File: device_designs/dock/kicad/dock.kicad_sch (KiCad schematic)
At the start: 16 parts, among them J1 USB_C_UPSTREAM, J2 USB_C_DS_x2, J3 USB_A_x2, J4 HDMI_or_DP, J5 RJ45, J6 RING_POGO, U1 JHL9040, U1A VL108, U2 TPS65994, U3 RTL8156, U4 VL817, U5 TPS55288RPMR, U6 TPS62864, U7 TLV75533PDRVR, U8 DWM3001C, U9 ALC4050

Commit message: fix(family): verify MPNs, freeze dock USB4/TB4, deepen mfg packages
Correct JHL9040R as TB4 retimer (not controller), freeze dock as USB4/TB4
40G with JHL8440, reject TB5, classify COM-HPC/NX5 pinout evidence, deepen
Gerber/STEP/PnP plans for all five, and document ring BOM↔FW parity.
KiCad brew needs Edmund admin — no COMPLETE claim.

Co-authored-by: Cursor <cursoragent@cursor.com>
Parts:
- added U1R: JHL9040R, symbol Device:R
- U1: value JHL9040 -> JHL8440; Role USB4_CONTROLLER -> USB4_TB4_DOCK_CONTROLLER
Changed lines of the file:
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@@
     (rev "0.2.0-dev")
     (company "gunnchOS3k / HARDWARE FAMILY DEPTH")
-    (comment 1 "ADR-FP-006 digital PCB package")
-    (comment 2 "USB4 + PD + hub + ring cradle")
+    (comment 1 "ADR-FP-006 + ADR-HW-002 USB4/TB4 40G NOT TB5")
+    (comment 2 "JHL8440 controller + JHL9040R retimer + PD + hub + cradle")
     (comment 3 "kicad-cli ABSENT → EDMUND_ACTION_REQUIRED")
     (comment 4 "PHYSICAL_EXECUTION_FREEZE ACTIVE — no fab, no purchase, draft digital only")
@@
     (in_bom yes) (on_board yes) (dnp no)
     (property "Reference" "U1" (at 40 33 0) (effects (font (size 1.27 1.27))))
-    (property "Value" "JHL9040" (at 40 47 0) (effects (font (size 1.27 1.27))))
+    (property "Value" "JHL8440" (at 40 47 0) (effects (font (size 1.27 1.27))))
     (property "Footprint" "" (at 40 40 0) (effects (font (size 1.27 1.27)) hide))
     (property "Datasheet" "" (at 40 40 0) (effects (font (size 1.27 1.27)) hide))
-    (property "Role" "USB4_CONTROLLER" (at 40 40 0) (effects (font (size 1.27 1.27)) hide))
+    (property "Role" "USB4_TB4_DOCK_CONTROLLER" (at 40 40 0) (effects (font (size 1.27 1.27)) hide))
+  )
+  (symbol (lib_id "Device:R") (at 65 40 0) (unit 1)
+    (in_bom yes) (on_board yes) (dnp no)
+    (property "Reference" "U1R" (at 65 33 0) (effects (font (size 1.27 1.27))))
+    (property "Value" "JHL9040R" (at 65 47 0) (effects (font (size 1.27 1.27))))
+    (property "Footprint" "" (at 65 40 0) (effects (font (size 1.27 1.27)) hide))
+    (property "Datasheet" "" (at 65 40 0) (effects (font (size 1.27 1.27)) hide))
+    (property "Role" "TB4_RETIMER" (at 65 40 0) (effects (font (size 1.27 1.27)) hide))
   )
   (symbol (lib_id "Device:R") (at 90 40 0) (unit 1)

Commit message: feat(eda): Cont VI KiCad 10.0.5 CLI validation + PCB load fixes
Install path resolved; run ERC/DRC/Gerber/drill/PnP/STEP for all five boards.
Fix KiCad 10 PCB load blockers (unknown setup key on Student/DS-XL; odd
5-layer copper on Dock → 4-layer). Record RING_KICAD_CLI_VALIDATION_PASS
and honest per-board violation counts; NDA release posture unchanged.

Co-authored-by: Cursor <cursoragent@cursor.com>
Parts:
- removed J2: USB_C_DS_x2, symbol Device:R
- removed J3: USB_A_x2, symbol Device:R
- added FORBID1: JHL9480, symbol Device:R
- added FORBID2: JHL9580, symbol Device:R
- added J2A, J2B: USB4085, symbol Device:R
- added J3A, J3B: USB3_A, symbol Device:R
- J1: value USB_C_UPSTREAM -> USB4085
- J4: value HDMI_or_DP -> HDMI_TypeA
- J5: value RJ45 -> JK0-0136NL
- J6: value RING_POGO -> Mill-Max_pogo
- U2: value TPS65994 -> TPS65994ADFBRQ1
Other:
- company: gunnchOS3k / HARDWARE FAMILY DEPTH -> gunnchOS3k / CONTINUATION VI
- title: Dock Main PCB — beyond skeleton -> Dock Main PCB — USB4/TB4 40G topology

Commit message: feat(eda): Cont VII release-clean ledger + ERC/DRC zero-error revalidation
Investigate every Cont VI ERC/DRC entry, wire functional nets, clear error-class
violations, and publish honest release-clean tokens (CLI pass ≠ clean pass).

Co-authored-by: Cursor <cursoragent@cursor.com>
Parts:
- removed FORBID1: JHL9480, symbol Device:R
- removed FORBID2: JHL9580, symbol Device:R
- removed J1, J2A, J2B: USB4085, symbol Device:R
- removed J3A, J3B: USB3_A, symbol Device:R
- removed J4: HDMI_TypeA, symbol Device:R
- removed J5: JK0-0136NL, symbol Device:R
- removed J6: Mill-Max_pogo, symbol Device:R
- removed U1: JHL8440, symbol Device:R
- removed U1A: VL108, symbol Device:R
- removed U1R: JHL9040R, symbol Device:R
- removed U2: TPS65994ADFBRQ1, symbol Device:R
- removed U3: RTL8156, symbol Device:R
- removed U4: VL817, symbol Device:R
- removed U5: TPS55288RPMR, symbol Device:R
- removed U6: TPS62864, symbol Device:R
- removed U7: TLV75533PDRVR, symbol Device:R
- removed U8: DWM3001C, symbol Device:R
- removed U9: ALC4050, symbol Device:R
- added FORBID1: JHL9480, gunnchos_structural:Block_SMD_10x10, symbol FuncBlock
- added FORBID2: JHL9580, gunnchos_structural:Block_SMD_10x10, symbol FuncBlock
- added J1, J2A, J2B: USB4085, gunnchos_structural:Block_SMD_10x10, symbol FuncBlock
- added J3A, J3B: USB3_A, gunnchos_structural:Block_SMD_10x10, symbol FuncBlock
- added J4: HDMI_TypeA, gunnchos_structural:Block_SMD_10x10, symbol FuncBlock
- added J5: JK0-0136NL, gunnchos_structural:Block_SMD_10x10, symbol FuncBlock
- added J6: Mill-Max_pogo, gunnchos_structural:Block_SMD_10x10, symbol FuncBlock
- added U1: JHL8440, gunnchos_structural:Block_SMD_10x10, symbol FuncBlock
- added U1A: VL108, gunnchos_structural:Block_SMD_10x10, symbol FuncBlock
- added U1R: JHL9040R, gunnchos_structural:Block_SMD_10x10, symbol FuncBlock
- added U2: TPS65994ADFBRQ1, gunnchos_structural:Block_SMD_10x10, symbol FuncBlock
- added U3: RTL8156, gunnchos_structural:Block_SMD_10x10, symbol FuncBlock
- added U4: VL817, gunnchos_structural:Block_SMD_10x10, symbol FuncBlock
- added U5: TPS55288RPMR, gunnchos_structural:Block_SMD_10x10, symbol FuncBlock
- added U6: TPS62864, gunnchos_structural:Block_SMD_10x10, symbol FuncBlock
- added U7: TLV75533PDRVR, gunnchos_structural:Block_SMD_10x10, symbol FuncBlock
- added U8: DWM3001C, gunnchos_structural:Block_SMD_10x10, symbol FuncBlock
- added U9: ALC4050, gunnchos_structural:Block_SMD_10x10, symbol FuncBlock
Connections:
- net CC1: now also J3A.2
- net CC2: now also J3B.2
- net HDMI_TX: now also U1.1
- net I2C_PD: now also J4.2
- net I2C_RETIMER: now also J5.2
- net MDI: now also FORBID2.2
- net RING_CHARGE_5V: now also U1R.1
- net SPI_UWB: now also U1A.1
- net SS_RX_DS1: now also J1.2
- net SS_RX_DS2: now also J2B.2
- net SS_RX_HOST: now also U6.2
- net SS_RX_UP: now also U8.2
- net SS_TX_DS1: now also U9.2
- net SS_TX_DS2: now also J2A.2
- net SS_TX_HOST: now also U5.2
- net SS_TX_UP: now also U7.2
- net USB_A1: now also J6.2
- net USB_A2: now also FORBID1.2
- net VBUS_DS1: now also U1R.2
- net VBUS_DS2: now also U1A.2
- net VBUS_UPSTREAM: now also U1.2
- net VDD_1V8: now also U4.2
- net VDD_3V3: now also U3.2
- net VSYS_5V: now also U2.2
- no-connect marks 0 -> 18
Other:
- company: gunnchOS3k / CONTINUATION VI -> gunnchOS3k / CONTINUATION VII
- title: Dock Main PCB — USB4/TB4 40G topology -> Dock Main PCB — USB4/TB4 Cont VII

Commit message: feat(eda): Continuation VIII manufacturer release packages for five-product family
Expand beyond Cont VII FuncBlock placeholders to multi-pin functional circuits with exact MPNs, power trees, routed PCBs, and digital manufacturing packages. Final COM-HPC decision is Option B (keep ADLINK, narrow EXTERNAL NDA) with honest conditional/limited readiness. ERC/DRC errors are zero on all five boards under KiCad 10.0.5; PHYSICAL_EXECUTION_FREEZE remains active.

Co-authored-by: Cursor <cursoragent@cursor.com>
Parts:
- removed FORBID1: JHL9480, gunnchos_structural:Block_SMD_10x10, symbol FuncBlock
- removed FORBID2: JHL9580, gunnchos_structural:Block_SMD_10x10, symbol FuncBlock
- removed J1, J2A, J2B: USB4085, gunnchos_structural:Block_SMD_10x10, symbol FuncBlock
- removed J3A, J3B: USB3_A, gunnchos_structural:Block_SMD_10x10, symbol FuncBlock
- removed J4: HDMI_TypeA, gunnchos_structural:Block_SMD_10x10, symbol FuncBlock
- removed J5: JK0-0136NL, gunnchos_structural:Block_SMD_10x10, symbol FuncBlock
- removed J6: Mill-Max_pogo, gunnchos_structural:Block_SMD_10x10, symbol FuncBlock
- removed U1: JHL8440, gunnchos_structural:Block_SMD_10x10, symbol FuncBlock
- removed U1A: VL108, gunnchos_structural:Block_SMD_10x10, symbol FuncBlock
- removed U1R: JHL9040R, gunnchos_structural:Block_SMD_10x10, symbol FuncBlock
- removed U2: TPS65994ADFBRQ1, gunnchos_structural:Block_SMD_10x10, symbol FuncBlock
- removed U3: RTL8156, gunnchos_structural:Block_SMD_10x10, symbol FuncBlock
- removed U4: VL817, gunnchos_structural:Block_SMD_10x10, symbol FuncBlock
- removed U5: TPS55288RPMR, gunnchos_structural:Block_SMD_10x10, symbol FuncBlock
- removed U6: TPS62864, gunnchos_structural:Block_SMD_10x10, symbol FuncBlock
- removed U7: TLV75533PDRVR, gunnchos_structural:Block_SMD_10x10, symbol FuncBlock
- removed U8: DWM3001C, gunnchos_structural:Block_SMD_10x10, symbol FuncBlock
- removed U9: ALC4050, gunnchos_structural:Block_SMD_10x10, symbol FuncBlock
- added C1: CL05A104KA5NNNC, gunnchos_functional:C_0402, symbol C
- added C2: GRM188R60J106ME47D, gunnchos_functional:C_0402, symbol C
- added D1: APTD1608LCGCK, gunnchos_functional:LED_0603, symbol LED
- added DESD1: PESD5V0S1UL, gunnchos_functional:R_0402, symbol C
- added JUSB1, JUSB2: TYPE-C-31-M-12, gunnchos_functional:Block_SMD_safe, symbol USB_C
- added R1: RC0402FR-0710KL, gunnchos_functional:R_0402, symbol R
- added R2: RC0402FR-071K0L, gunnchos_functional:R_0402, symbol R
- added U3V3: TPS62864, gunnchos_functional:Block_SMD_safe, symbol BUCK
- added UCHG1: BQ25792RQMR, gunnchos_functional:Block_SMD_safe, symbol CHARGER
- added UETH1: RTL8156, gunnchos_functional:Block_SMD_safe, symbol RTL8156
- added UHUB1: VL817, gunnchos_functional:Block_SMD_safe, symbol VL817
- added UPD1: TPS65994ADFBRQ1, gunnchos_functional:Block_SMD_safe, symbol PD_CTRL
- added UUSB4: JHL8440, gunnchos_functional:Block_SMD_safe, symbol JHL8440_ROLE
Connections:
- net CC1: now also DESD1.1, JUSB1.A5 (CC1), UPD1.8 (3V3)
- net VDD_3V3: now also C1.1, R1.1, R2.1, U3V3.2 (EN), U3V3.4 (VOUT), UETH1.7 (RD+), UHUB1.5 (DN1_DP), UPD1.2 (CC1), UUSB4.9 (NOTE_NDA)
- new net ETH_TD_N: UETH1.4 (USB_D-)
- new net ETH_TD_P: UETH1.3 (USB_D+)
- new net GND: C1.2, C2.2, D1.1 (K), DESD1.2, JUSB1.A7 (DM), JUSB2.A7 (DM), U3V3.1 (VIN), UCHG1.4 (GND), UETH1.8 (RD-), UHUB1.6 (DN1_DM), UPD1.6 (SDA), UUSB4.8 (I2C_SDA)
- new net HUB_DN1_DM: JUSB2.A1 (GND), UHUB1.2 (GND)
- new net HUB_DN1_DP: JUSB2.A6 (DP), UHUB1.1 (VDD)
- new net I2C_SCL: R1.2, UCHG1.1 (VBUS), UPD1.3 (CC2), UUSB4.3 (USB4_UP_RX)
- new net I2C_SDA: UCHG1.2 (SYS), UPD1.4 (GND), UUSB4.2 (GND)
- new net LED_A: D1.2 (A), R2.2
- new net USB4_UP: UUSB4.6 (PCIE_DN), UUSB4.7 (I2C_SCL)
- new net USB_DM: UETH1.6 (TD-), UHUB1.4 (UP_DM)
- new net USB_DP: UETH1.5 (TD+), UHUB1.3 (UP_DP)
- new net VBAT: UCHG1.3 (BAT)
- new net VBUS: JUSB1.B5 (CC2), JUSB2.B5 (CC2), UCHG1.5 (SCL), UPD1.7 (VSYS)
- new net VSYS: C2.1, U3V3.3 (GND), UCHG1.6 (SDA), UPD1.1 (VBUS)
- no-connect marks 18 -> 11
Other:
- note added: "Cont VIII functional schematic — multi-pin symbols + exact MPNs (not FuncBlock placeholders)."
- note added: "EXTERNAL_NDA_BLOCKED: Intel JHL8440 / JHL9040R package ball maps"
- note added: "Revision 0.5.0-cont-viii."
- note added: "SI notes encoded on PCB stackup/Dwgs — no SI simulation claimed."
- company: gunnchOS3k / CONTINUATION VII -> gunnchOS3k / CONTINUATION VIII
- title: Dock Main PCB — USB4/TB4 Cont VII -> Dock Main PCB — USB4/TB4 Cont VIII

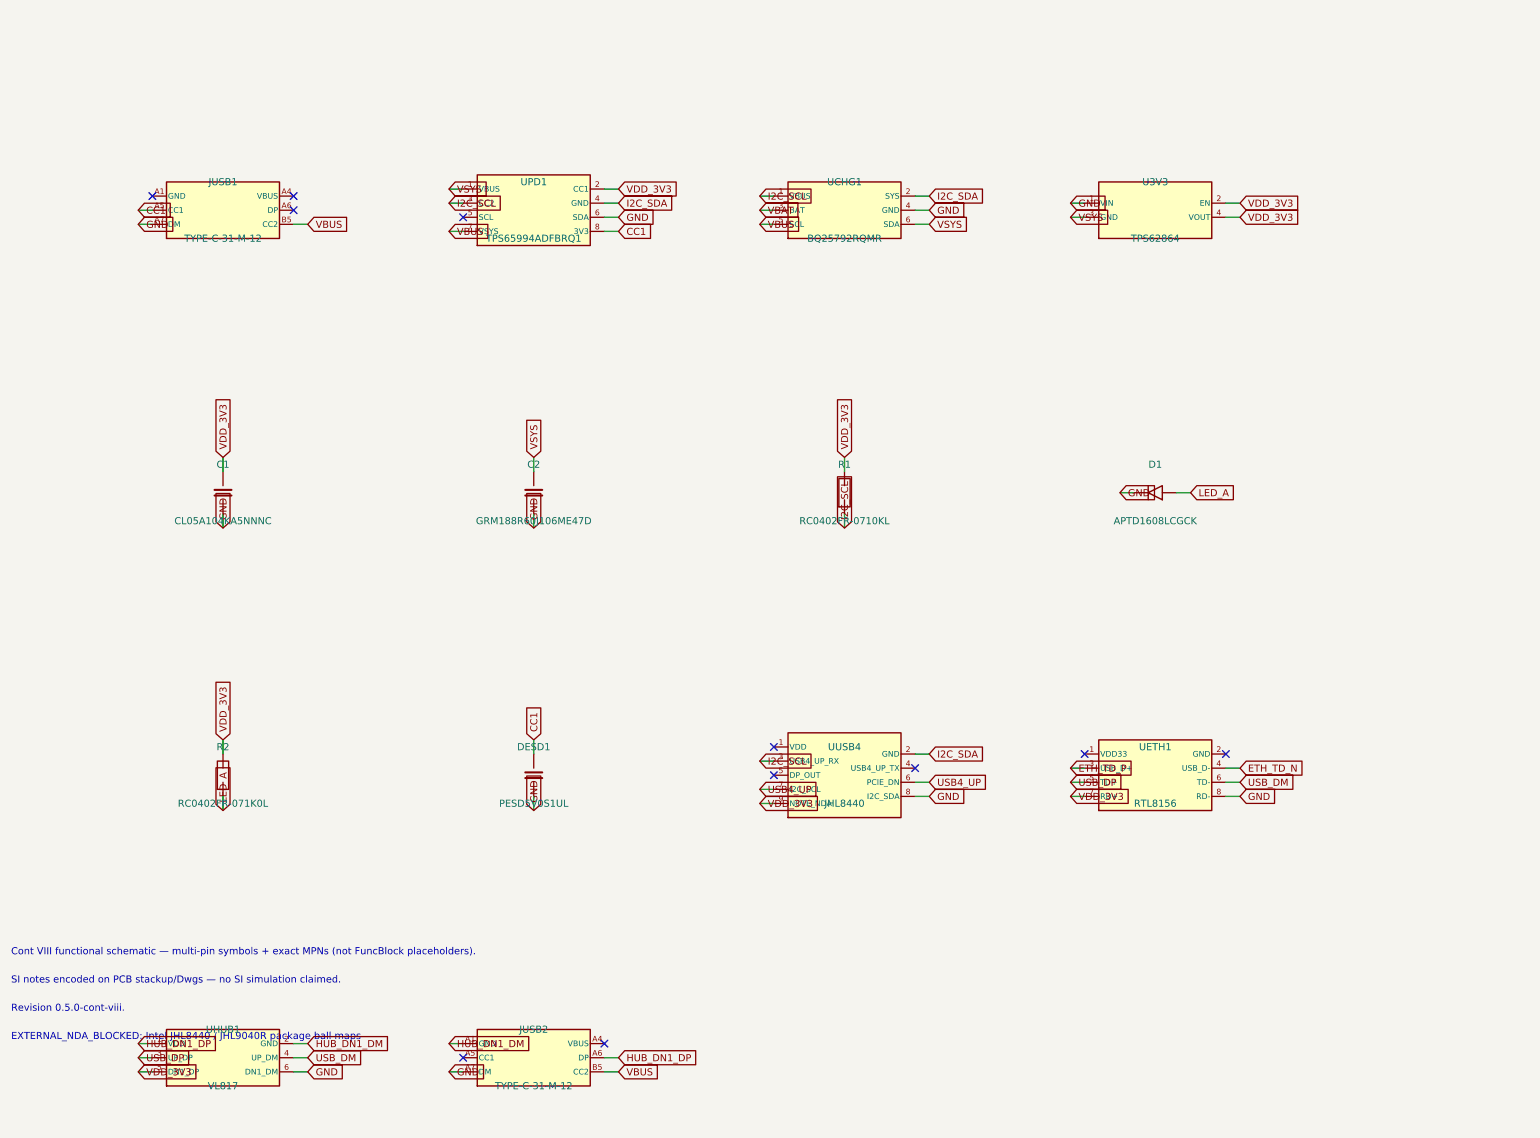
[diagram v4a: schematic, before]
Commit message: feat(eda): Continuation IX Pre-EVT digital release lock for five-product family
Close Cont VIII residual DIGITAL blockers with production footprints, full Radxa 260-pin hierarchical sheets, assembly/RFQ/EVT packages, and honest ADLINK-retained COM-HPC tokens under PHYSICAL_EXECUTION_FREEZE.

Co-authored-by: Cursor <cursoragent@cursor.com>
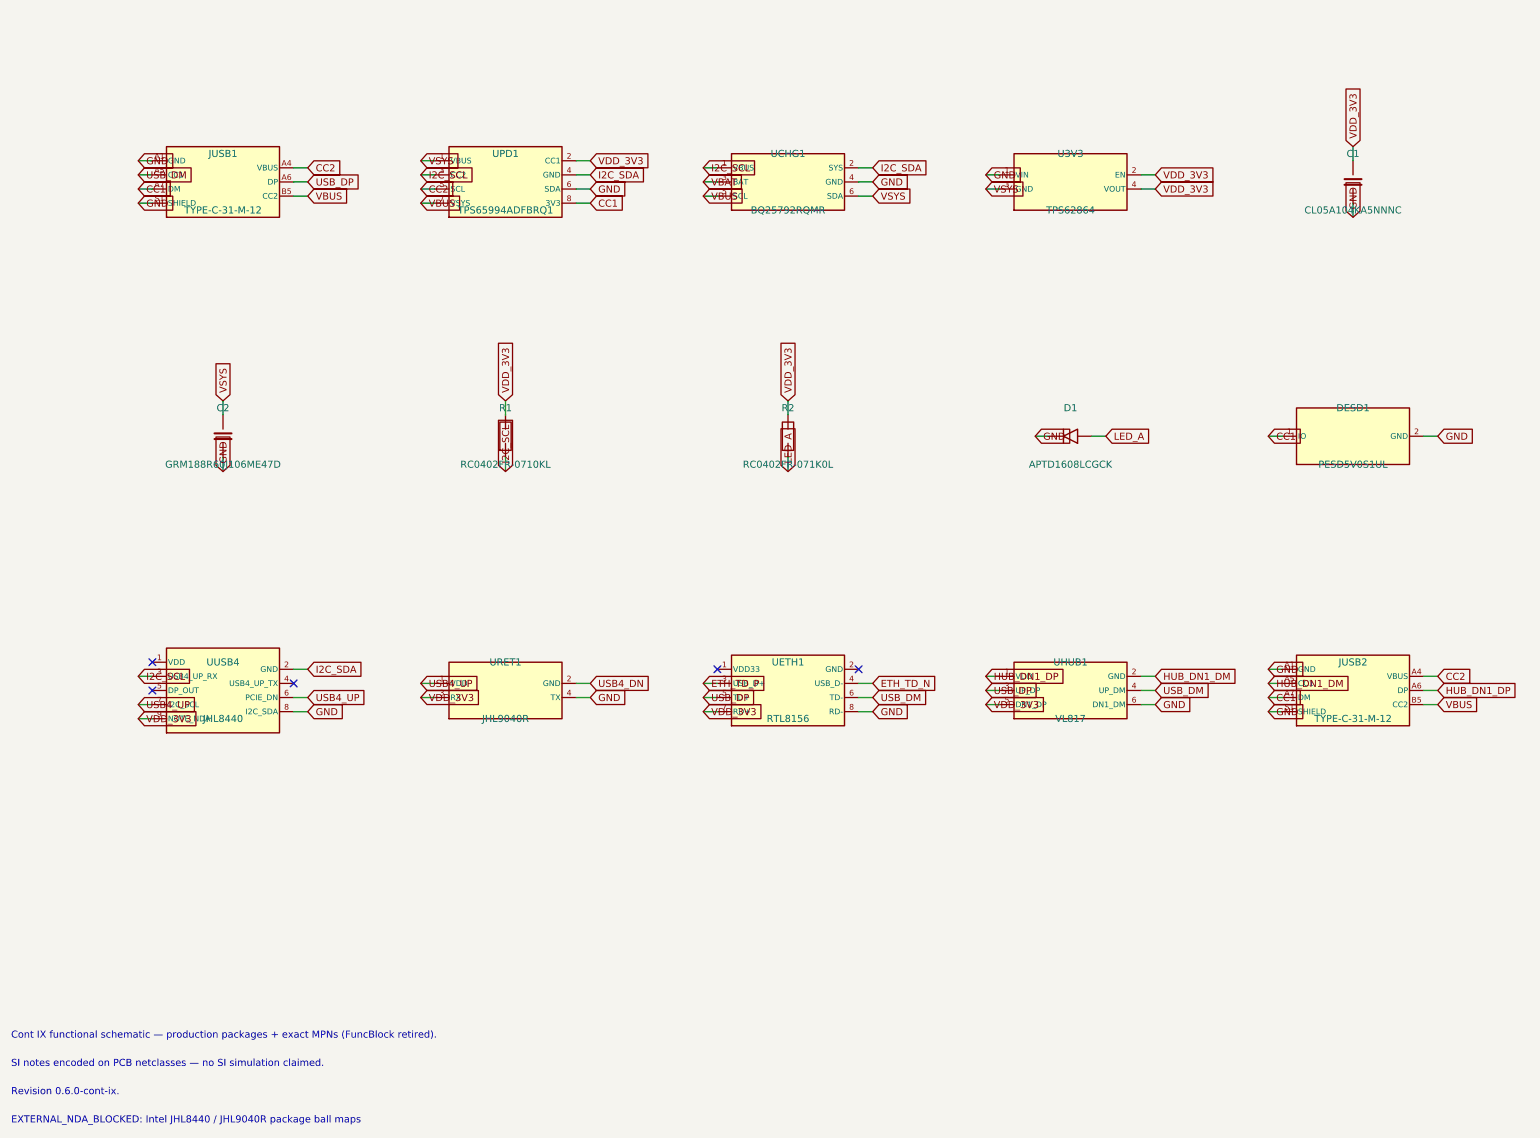
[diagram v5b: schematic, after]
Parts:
- added URET1: JHL9040R, gunnchos_production:JHL9040R_ROLE_envelope, symbol JHL9040R_ROLE
- C1, C2: footprint gunnchos_functional:C_0402 -> gunnchos_production:C_0402; ContIX (none) -> PRODUCTION; ContVIII FUNCTIONAL -> (none)
- D1: footprint gunnchos_functional:LED_0603 -> gunnchos_production:LED_0603; ContIX (none) -> PRODUCTION; ContVIII FUNCTIONAL -> (none)
- DESD1: footprint gunnchos_functional:R_0402 -> gunnchos_production:DFN1006-2; symbol C -> ESD; ContIX (none) -> PRODUCTION; ContVIII FUNCTIONAL -> (none)
- JUSB1, JUSB2: footprint gunnchos_functional:Block_SMD_safe -> gunnchos_production:USB_C_Receptacle_Production; ContIX (none) -> PRODUCTION; ContVIII FUNCTIONAL -> (none)
- R1, R2: footprint gunnchos_functional:R_0402 -> gunnchos_production:R_0402; ContIX (none) -> PRODUCTION; ContVIII FUNCTIONAL -> (none)
- U3V3: footprint gunnchos_functional:Block_SMD_safe -> gunnchos_production:QFN-16-1EP_3x3mm_P0.5mm; ContIX (none) -> PRODUCTION; ContVIII FUNCTIONAL -> (none)
- UCHG1: footprint gunnchos_functional:Block_SMD_safe -> gunnchos_production:WQFN-29-1EP_4x4mm_P0.4mm; ContIX (none) -> PRODUCTION; ContVIII FUNCTIONAL -> (none)
- UETH1: footprint gunnchos_functional:Block_SMD_safe -> gunnchos_production:QFN-48-1EP_6x6mm_P0.4mm; ContIX (none) -> PRODUCTION; ContVIII FUNCTIONAL -> (none)
- UHUB1: footprint gunnchos_functional:Block_SMD_safe -> gunnchos_production:QFN-48-1EP_7x7mm_P0.5mm; ContIX (none) -> PRODUCTION; ContVIII FUNCTIONAL -> (none)
- UPD1: footprint gunnchos_functional:Block_SMD_safe -> gunnchos_production:VQFN-48-1EP_7x7mm_P0.5mm; ContIX (none) -> PRODUCTION; ContVIII FUNCTIONAL -> (none)
- UUSB4: footprint gunnchos_functional:Block_SMD_safe -> gunnchos_production:JHL8440_ROLE_envelope; ContIX (none) -> PRODUCTION; ContVIII FUNCTIONAL -> (none)
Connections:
- net CC1: now also JUSB1.A7 (DM), JUSB2.A7 (DM); no longer JUSB1.A5 (CC1)
- net GND: now also JUSB1.A1 (GND), JUSB1.S1 (SHIELD), JUSB2.A1 (GND), JUSB2.S1 (SHIELD), URET1.4 (TX); no longer JUSB1.A7 (DM), JUSB2.A7 (DM)
- net HUB_DN1_DM: now also JUSB2.A5 (CC1); no longer JUSB2.A1 (GND)
- net USB4_UP: now also URET1.1 (VDD)
- net USB_DM: now also JUSB1.A5 (CC1)
- net USB_DP: now also JUSB1.A6 (DP)
- net VDD_3V3: now also URET1.3 (RX)
- net CC2: now reaches UPD1.5 (SCL)
- net CC2: now also JUSB1.A4 (VBUS), JUSB2.A4 (VBUS)
- new net USB4_DN: URET1.2 (GND)
- no-connect marks 11 -> 5
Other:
- note added: "Cont IX functional schematic — production packages + exact MPNs (FuncBlock retired)."
- note added: "Revision 0.6.0-cont-ix."
- note added: "SI notes encoded on PCB netclasses — no SI simulation claimed."
- note removed: "Cont VIII functional schematic — multi-pin symbols + exact MPNs (not FuncBlock placeholders)."
- note removed: "Revision 0.5.0-cont-viii."
- note removed: "SI notes encoded on PCB stackup/Dwgs — no SI simulation claimed."
- company: gunnchOS3k / CONTINUATION VIII -> gunnchOS3k / CONTINUATION IX
- title: Dock Main PCB — USB4/TB4 Cont VIII -> Dock Main PCB — USB4/TB4 Cont IX
- moved on the sheet: C1, C2, D1, R1, R2, U3V3, UCHG1, UETH1, UHUB1, UPD1, UUSB4
